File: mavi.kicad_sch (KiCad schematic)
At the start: 18 parts, among them J1 Input +V1, J2 Input -V1, U1 MCP6002-xP

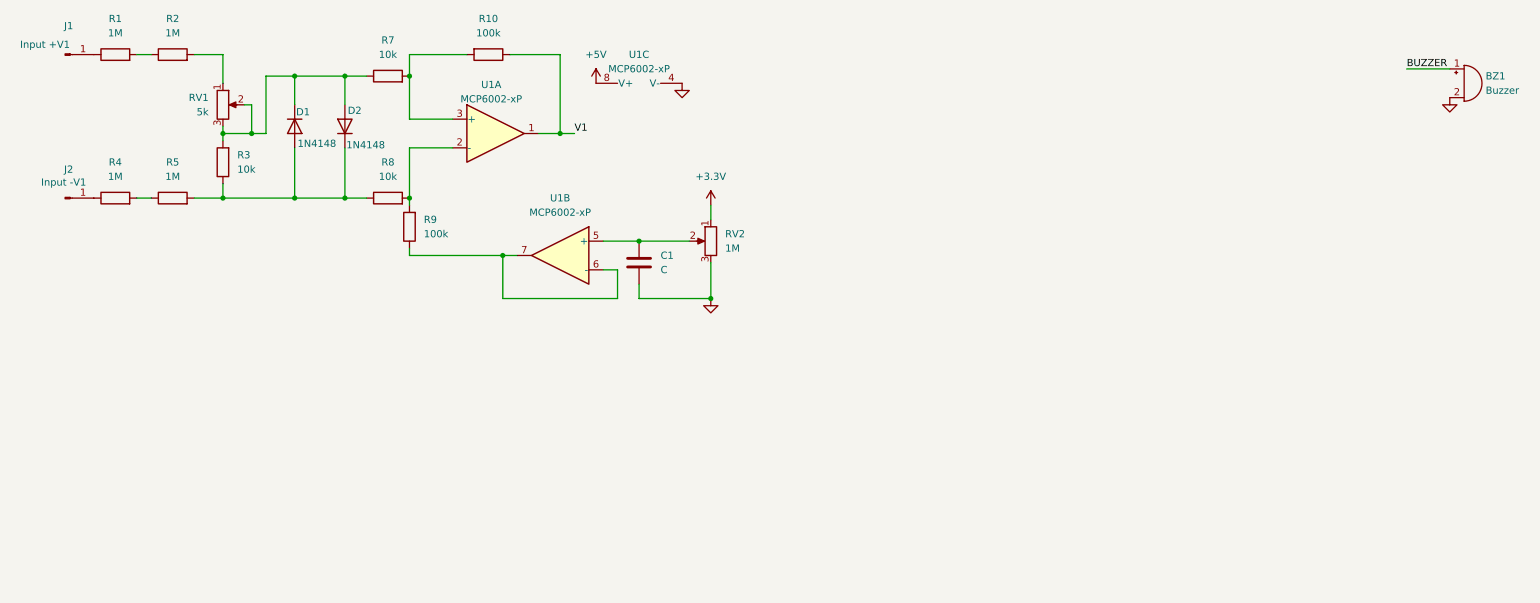
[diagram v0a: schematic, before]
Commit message: firmware connection
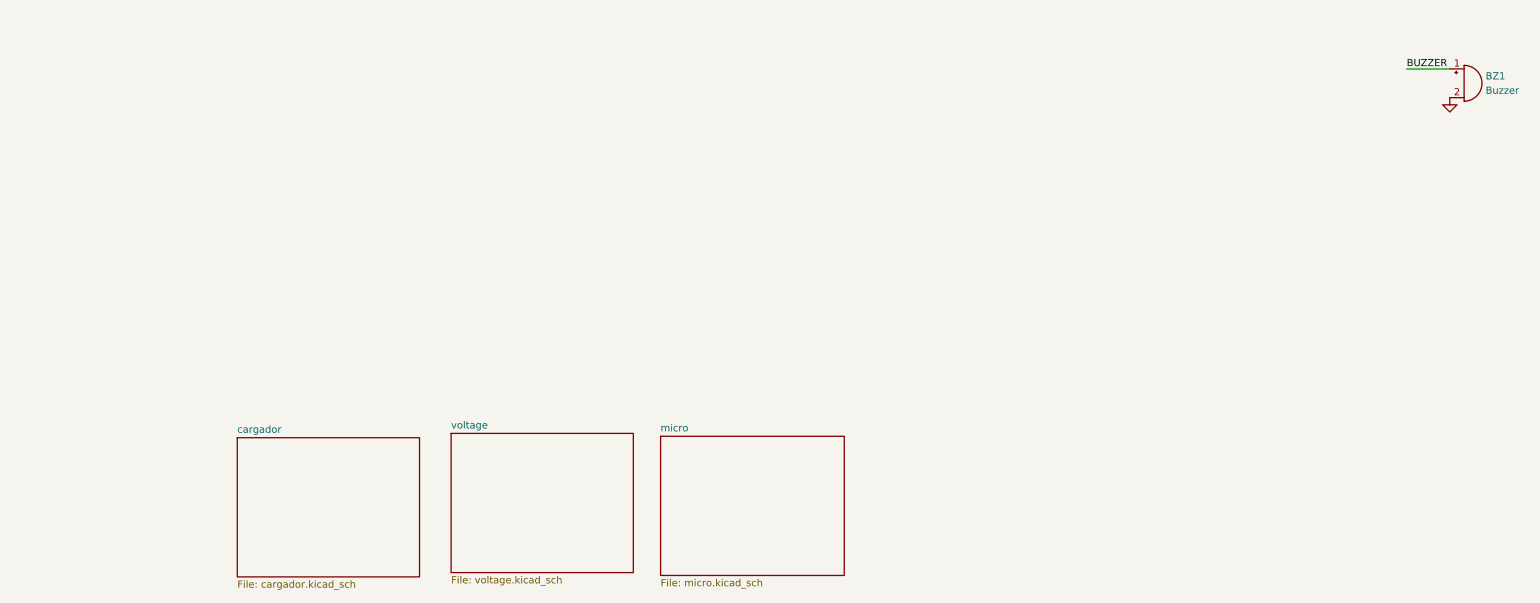
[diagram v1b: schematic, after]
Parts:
- removed C1: C, symbol Device:C
- removed D1, D2: 1N4148, Diode_THT:D_DO-35_SOD27_P7.62mm_Horizontal, symbol Diode:1N4148
- removed J1: Input +V1, symbol Connector:Conn_01x01_Pin
- removed J2: Input -V1, symbol Connector:Conn_01x01_Pin
- removed R1, R2, R4, R5: 1M, symbol Device:R
- removed R10, R9: 100k, symbol Device:R
- removed R3, R7, R8: 10k, symbol Device:R
- removed RV1: 5k, symbol Device:R_Potentiometer
- removed RV2: 1M, symbol Device:R_Potentiometer
- removed U1: MCP6002-xP, symbol Amplifier_Operational:MCP6002-xP
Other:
- added sheet cargador (cargador.kicad_sch)
- added sheet micro (micro.kicad_sch)
- added sheet voltage (voltage.kicad_sch)
